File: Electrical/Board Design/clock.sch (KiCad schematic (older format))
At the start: 51 parts, among them CON1 AVR-ISP-6, CON2 USB-MICRO-B, IC1 ATTINY84A-SS, P1 CONN_6, P2 CONN_2, P3 CONN_2, P4 CONN_2, Q1 FET_N, Q2 FET_P, SW1 SPST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

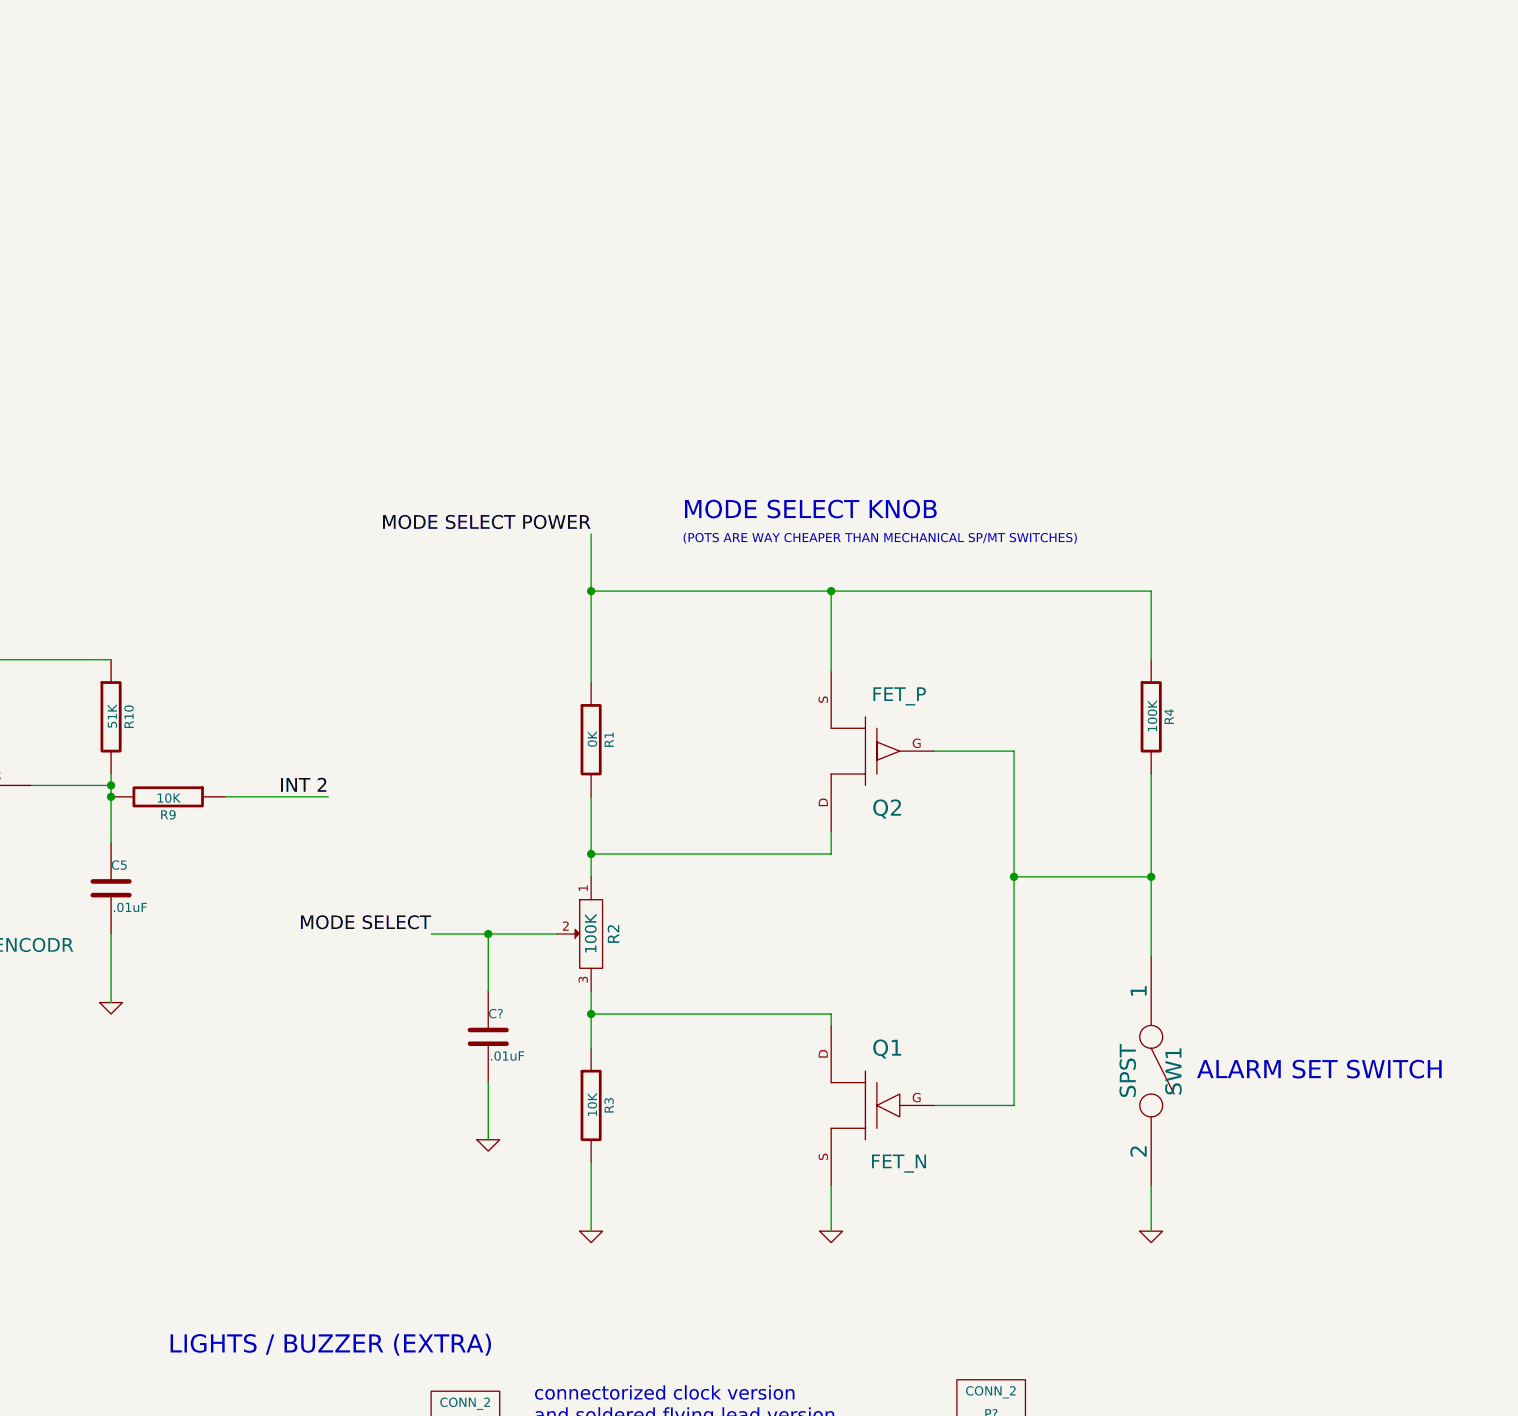
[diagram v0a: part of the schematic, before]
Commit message: closes issue 19, shortable pullup
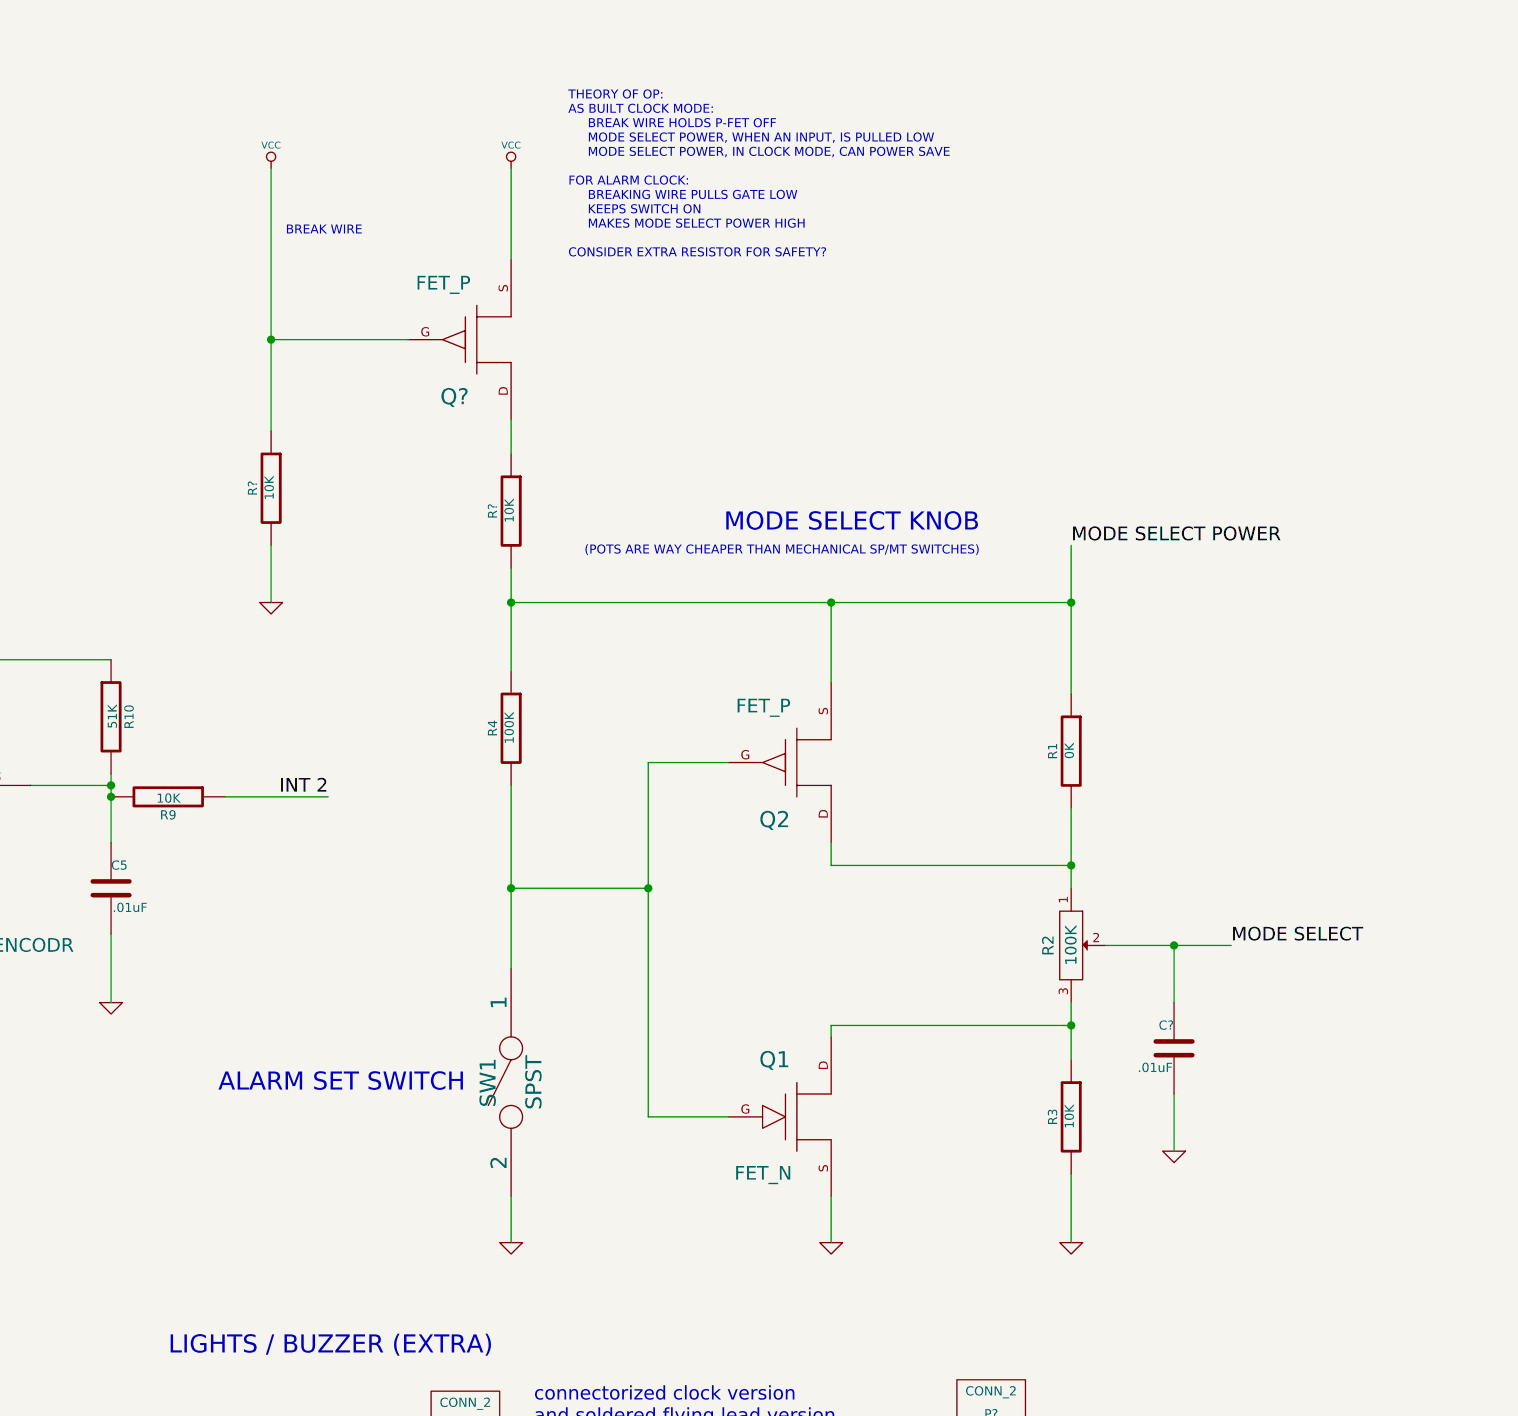
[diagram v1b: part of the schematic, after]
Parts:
- added Q?: FET_P, ~, symbol FET_P
- added R? (x2): 10K, ~, symbol R
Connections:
- wire segments 167 -> 172
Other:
- note added: "BREAK WIRE\n"
- note added: "THEORY OF OP:\nAS BUILT CLOCK MODE:\n BREAK WIRE HOLDS P-FET OFF\n MODE SELECT POWER, WHEN AN INPUT, IS PULLED LOW\n MODE SELECT POWER, IN CLOCK MODE, CAN POWER SAVE\n\nFOR ALARM CLOCK:\n BREAKING WIRE PULLS GATE LOW\n KEEPS SWITCH ON\n MAKES MODE SELECT POWER HIGH\n\nCONSIDER EXTRA RESISTOR FOR SAFETY?"
- moved on the sheet: C?, Q1, Q2, R1, R2, R3, R4, SW1

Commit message: changed breakaway to a capacitor solution
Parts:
- removed Q?: FET_P, ~, symbol FET_P
- removed R? (x2): 10K, ~, symbol R
- added C?: 10uF, ~, symbol C
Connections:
- wire segments 172 -> 213
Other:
- note added: "BREAK TAB\n"
- note added: "THEORY OF OP:\nAS BUILT CLOCK MODE:\n CAPACITOR HOLDS CHARGE LONG ENOUGH TO DETECT HIGH\n\nFOR ALARM CLOCK:\n BREAKING WIRE DISCONNECTS CAPACTOR\n OUTPUT IS PULLED LOW\n"
- note removed: "BREAK WIRE\n"
- note removed: "THEORY OF OP:\nAS BUILT CLOCK MODE:\n BREAK WIRE HOLDS P-FET OFF\n MODE SELECT POWER, WHEN AN INPUT, IS PULLED LOW\n MODE SELECT POWER, IN CLOCK MODE, CAN POWER SAVE\n\nFOR ALARM CLOCK:\n BREAKING WIRE PULLS GATE LOW\n KEEPS SWITCH ON\n MAKES MODE SELECT POWER HIGH\n\nCONSIDER EXTRA RESISTOR FOR SAFETY?"
- moved on the sheet: C?, Q1, Q2, R1, R2, R3, R4, SW1

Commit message: foot print and schematic updates
got the LED TE connector, SMT LDO, transistor for AM/PM lights
footprints and schematic updated
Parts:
- added Q3, Q4: FET_N, ~, symbol FET_N
- added U3: MCP1702T-1502E/CB, TO-92, symbol MCP1702T-1502E/CB
- gave numbers to parts that had none: 5
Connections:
- net labels added: +5V
- wire segments 213 -> 175
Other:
- moved on the sheet: C7, D1, D2, D3, P5, P6, R13, R14, R15, SP1, U2

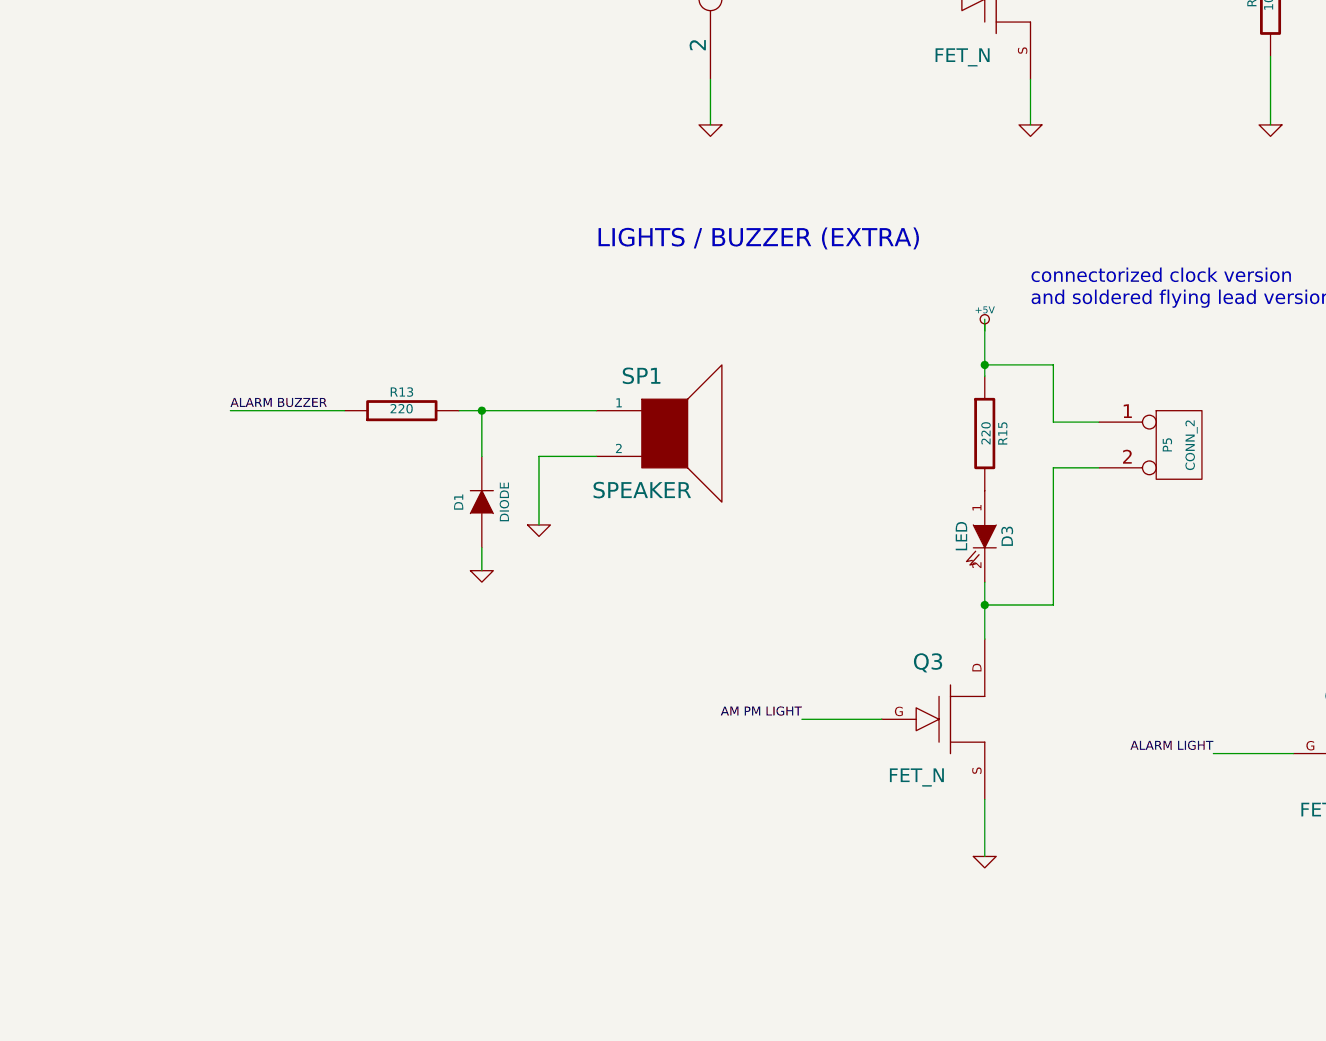
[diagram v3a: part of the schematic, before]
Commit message: made changes to speaker footprint
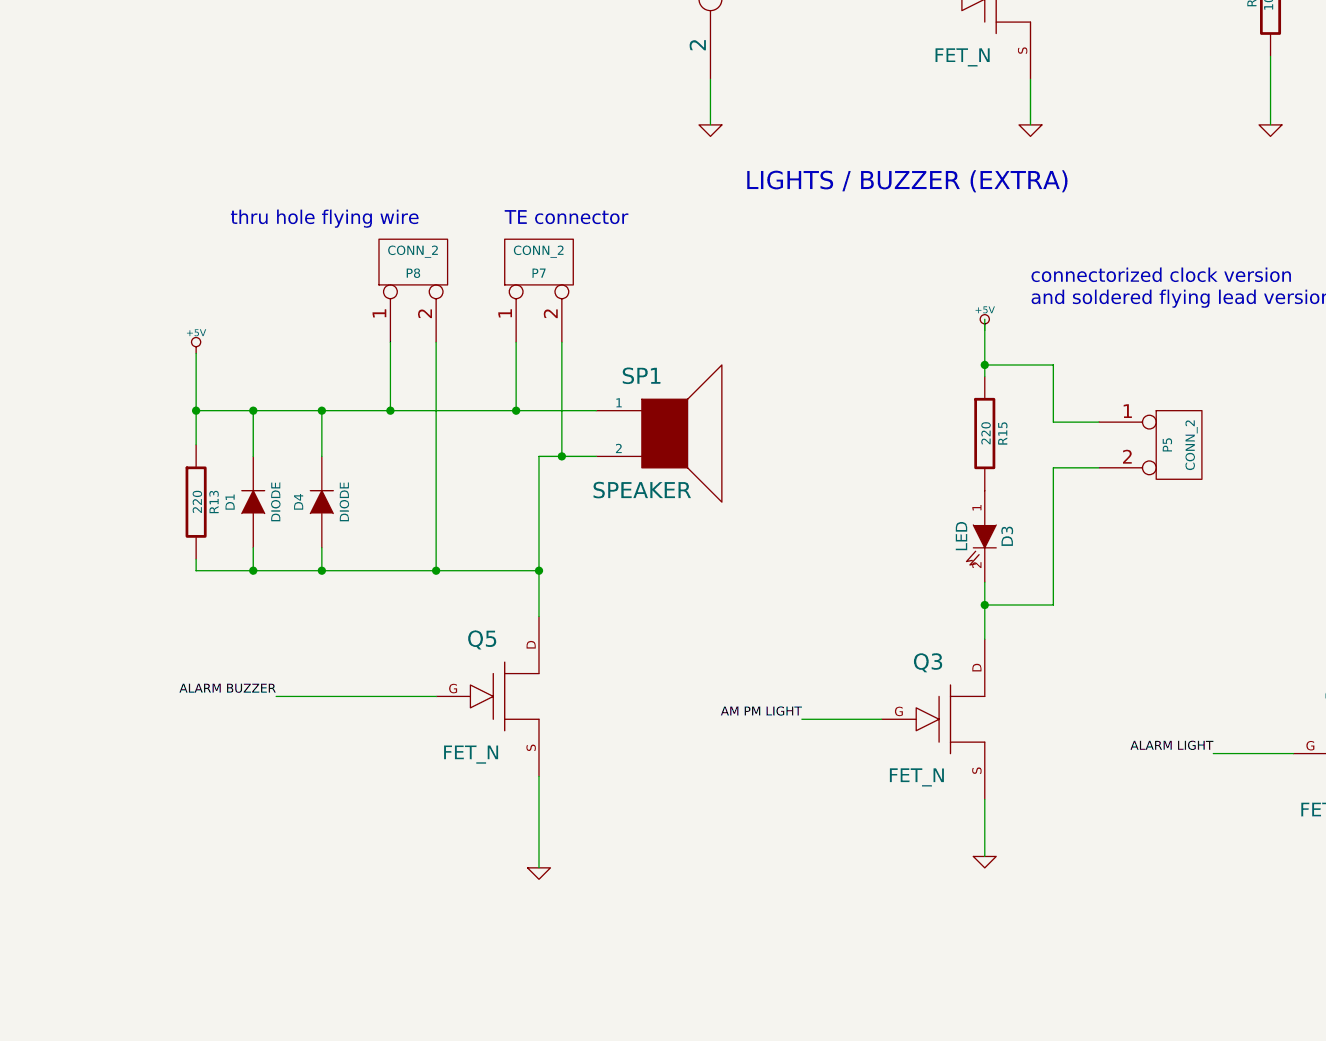
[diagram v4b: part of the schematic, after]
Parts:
- added D4: DIODE, ~, symbol DIODE
- added P7, P8: CONN_2, symbol CONN_2
- added Q5: FET_N, ~, symbol FET_N
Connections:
- wire segments 175 -> 185
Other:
- note added: "TE connector"
- note added: "thru hole flying wire"
- moved on the sheet: D1

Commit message: reorganized board layout, but haven't fully wired
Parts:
- added C10: 1uF, ~, symbol C
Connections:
- wire segments 185 -> 187
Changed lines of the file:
@@
 Sheet 1 1
 Title ""
-Date "4 nov 2015"
+Date "9 nov 2015"
 Rev ""
 Comp ""
@@
 F 3 "~" H 14650 4850 60  0000 C CNN
 	1    14650 4850
-	0    1    1    0
+	0    1    -1   0
 $EndComp
 Text Notes 12000 5500 2    79   ~ 0
@@
 	10500 8000 10500 8100
 Connection ~ 10500 8100
+$Comp
+L C C10
+U 1 1 5640BA9C
+P 3600 1750
+F 0 "C10" H 3600 1850 40  0000 L CNN
+F 1 "1uF" H 3606 1665 40  0000 L CNN
+F 2 "~" H 3638 1600 30  0000 C CNN
+F 3 "~" H 3600 1750 60  0000 C CNN
+	1    3600 1750
+	1    0    0    -1
+$EndComp
+Wire Wire Line
+	3600 1550 3600 1400
+Connection ~ 3600 1400
+Wire Wire Line
+	3600 1950 3600 2100
+Connection ~ 3600 2100
 $EndSCHEMATC

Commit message: finalized changes and sent to fab
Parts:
- added P9: CONN_2, symbol CONN_2
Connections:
- wire segments 187 -> 193
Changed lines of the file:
@@
 Sheet 1 1
 Title ""
-Date "9 nov 2015"
+Date "12 nov 2015"
 Rev ""
 Comp ""
@@
 L +5V #PWR034
 U 1 1 5636582A
-P 13400 7050
-F 0 "#PWR034" H 13400 7140 20  0001 C CNN
-F 1 "+5V" H 13400 7140 30  0000 C CNN
-F 2 "" H 13400 7050 60  0000 C CNN
-F 3 "" H 13400 7050 60  0000 C CNN
-	1    13400 7050
+P 13400 7000
+F 0 "#PWR034" H 13400 7090 20  0001 C CNN
+F 1 "+5V" H 13400 7090 30  0000 C CNN
+F 2 "" H 13400 7000 60  0000 C CNN
+F 3 "" H 13400 7000 60  0000 C CNN
+	1    13400 7000
 	1    0    0    -1
 $EndComp
@@
 	3600 1950 3600 2100
 Connection ~ 3600 2100
+$Comp
+L CONN_2 P9
+U 1 1 5643F12B
+P 11500 5750
+F 0 "P9" V 11450 5750 40  0000 C CNN
+F 1 "CONN_2" V 11550 5750 40  0000 C CNN
+F 2 "" H 11500 5750 60  0000 C CNN
+F 3 "" H 11500 5750 60  0000 C CNN
+	1    11500 5750
+	-1   0    0    1
+$EndComp
+Wire Wire Line
+	11850 5850 12050 5850
+Wire Wire Line
+	12050 5850 12050 6050
+Wire Wire Line
+	12050 6050 12200 6050
+Connection ~ 12200 6050
+Wire Wire Line
+	11850 5650 12000 5650
+Wire Wire Line
+	12000 5650 12000 4750
+Wire Wire Line
+	12000 4750 12200 4750
+Connection ~ 12200 4750
+Text Notes 14050 7800 0    60   ~ 0
+TE connector
+Text Notes 15700 7800 0    60   ~ 0
+TE connector
+Text Notes 11250 6000 0    60   ~ 0
+TE connector
 $EndSCHEMATC

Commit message: changed LED backlight power source, simplified POT, added LED dimming
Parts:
- removed C9: 10uF, ~, symbol C
- removed Q1: FET_N, ~, symbol FET_N
- removed Q2: FET_P, ~, symbol FET_P
- added C?: .01uF, ~, symbol C
- added P? (x2): CONN_2, symbol CONN_2
- added R?: 100K, ~, symbol POT
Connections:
- net +5V: now also R?.3
- net GND: now also P?.2 (PM), P?.2 (PM), R?.1
- net VCC: no longer P2.1 (P1), P3.1 (P1)
- net at P9.2 (PM), SW1.1: now also C?.2; no longer R4.2
- new net: C?.1, R4.2
- new net: P2.1 (P1), P3.1 (P1), P?.1 (P1), P?.1 (P1), R?.2
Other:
- note added: "THEORY OF OP:\n\nFOR THE BASE CLOCK, CAP IS DISCONNECTED, NO CHANGE\n\nFOR THE ALARM CLOCK, CAP HOLDS CHARGE, MODE SELECT POWER\nIS USED AS A GPIO TO BOTH CHARGE UP, AND MEASURE RESIDUAL CHARGE\nON, THE BOARD, BUT ONLY WHEN SWITCH IS CLOSED."
- note removed: "BREAK TAB\n"
- note removed: "THEORY OF OP:\nAS BUILT CLOCK MODE:\n CAPACITOR HOLDS CHARGE LONG ENOUGH TO DETECT HIGH\n\nFOR ALARM CLOCK:\n BREAKING WIRE DISCONNECTS CAPACTOR\n OUTPUT IS PULLED LOW\n"
- moved on the sheet: C8, P2, P3, R1, R2, R3, R4
